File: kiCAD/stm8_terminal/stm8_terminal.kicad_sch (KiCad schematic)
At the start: 26 parts, among them J1 USB_A, J2 PS/2 Female, J3 TV out, SW1 SW_SPST, SW2 local echo, SW3 baud rate 1, SW4 baud rate 0, T1 step down transformer, U1 LD1117V50-TO-220, Y1 20 Mhz

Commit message: Modification à la schématique
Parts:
- removed C2: 100nF, symbol Device:C
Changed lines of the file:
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@@
-    (pin "2")
-  )
-  (symbol (lib_id "Device:C") (at 128.27 114.3 0) (unit 1)
-    (in_bom yes) (on_board yes) (fields_autoplaced)
-    (property "Reference" "C2" (id 0) (at 131.445 113.0299 0)
-      (effects (font (size 1.27 1.27)) (justify left))
-    )
-    (property "Value" "100nF" (id 1) (at 131.445 115.5699 0)
-      (effects (font (size 1.27 1.27)) (justify left))
-    )
-    (property "Footprint" "" (id 2) (at 129.2352 118.11 0)
-      (effects (font (size 1.27 1.27)) hide)
-    )
-    (property "Datasheet" "~" (id 3) (at 128.27 114.3 0)
-      (effects (font (size 1.27 1.27)) hide)
-    )
-    (pin "1")
     (pin "2")
   )
@@
     (pin "1")
   )
-  (symbol (lib_id "power:GND") (at 128.27 118.11 0) (unit 1)
-    (in_bom yes) (on_board yes) (fields_autoplaced)
-    (property "Reference" "#PWR05" (id 0) (at 128.27 124.46 0)
-      (effects (font (size 1.27 1.27)) hide)
-    )
-    (property "Value" "GND" (id 1) (at 128.27 123.19 0))
-    (property "Footprint" "" (id 2) (at 128.27 118.11 0)
-      (effects (font (size 1.27 1.27)) hide)
-    )
-    (property "Datasheet" "" (id 3) (at 128.27 118.11 0)
-      (effects (font (size 1.27 1.27)) hide)
-    )
-    (pin "1")
-  )
   (symbol (lib_id "Device:C_Polarized") (at 112.395 55.88 0) (unit 1)
     (in_bom yes) (on_board yes) (fields_autoplaced)
@@
       (reference "#PWR04") (unit 1) (value "GND") (footprint "")
     )
-    (path "/845855d3-4d0e-4980-8991-a5f84e6b7908"
-      (reference "#PWR05") (unit 1) (value "GND") (footprint "")
-    )
     (path "/d18cab06-a3b9-490f-bba2-3968ae23ef3a"
       (reference "#PWR06") (unit 1) (value "GND") (footprint "")
@@
       (reference "C1") (unit 1) (value "4700µF/25V") (footprint "")
     )
-    (path "/141ad850-4428-4f02-9634-53c9c9f30976"
-      (reference "C2") (unit 1) (value "100nF") (footprint "")
-    )
     (path "/e24a0cb3-c996-41e3-aea6-3ef71e605019"

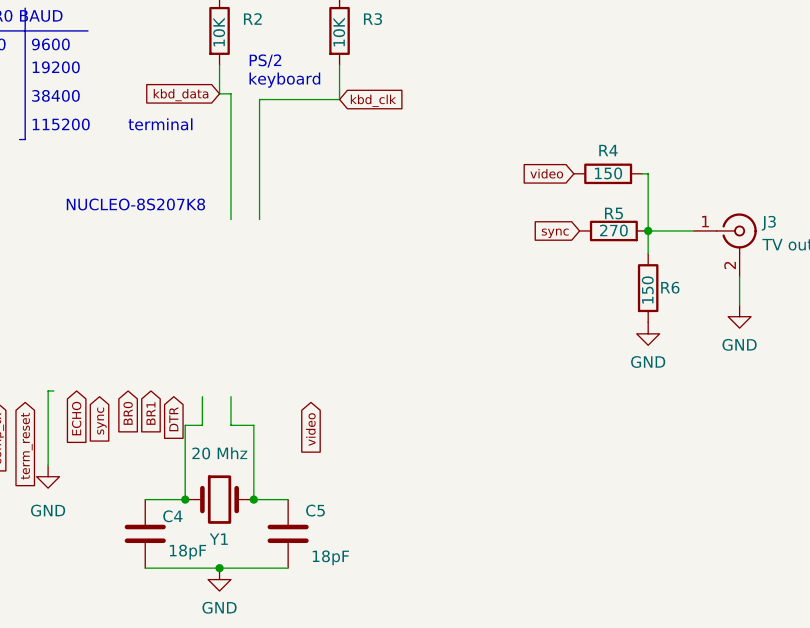
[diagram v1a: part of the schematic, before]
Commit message: mise à jour schématique vers V1.1R0
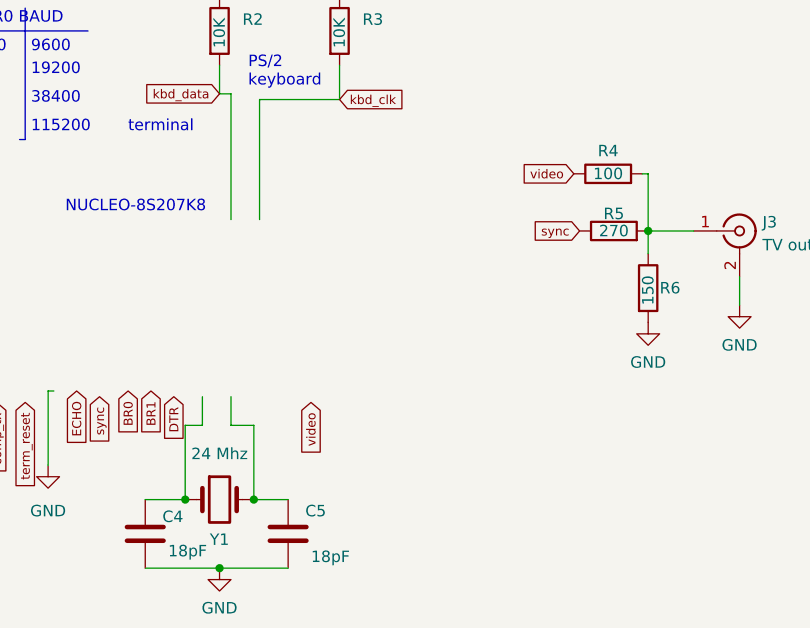
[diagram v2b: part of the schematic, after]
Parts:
- R4: value 150 -> 100
- Y1: value 20 Mhz -> 24 Mhz
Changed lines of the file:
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@@
     (in_bom yes) (on_board yes)
     (property "Reference" "R4" (id 0) (at 254.635 78.74 90))
-    (property "Value" "150" (id 1) (at 254.635 81.28 90))
+    (property "Value" "100" (id 1) (at 254.635 81.28 90))
     (property "Footprint" "" (id 2) (at 254.635 83.058 90)
       (effects (font (size 1.27 1.27)) hide)
@@
     (in_bom yes) (on_board yes)
     (property "Reference" "Y1" (id 0) (at 211.455 121.92 0))
-    (property "Value" "20 Mhz" (id 1) (at 211.455 112.395 0))
+    (property "Value" "24 Mhz" (id 1) (at 211.455 112.395 0))
     (property "Footprint" "" (id 2) (at 211.455 117.475 0)
       (effects (font (size 1.27 1.27)) hide)
@@
     )
     (path "/26747773-3488-4cb1-8229-30ef1aeade7f"
-      (reference "R4") (unit 1) (value "150") (footprint "")
+      (reference "R4") (unit 1) (value "100") (footprint "")
     )
     (path "/b67ff7bf-f5af-4273-8904-9679f573e1a3"
@@
     )
     (path "/a798556e-a1c1-4369-8d5b-478f85bd9f5b"
-      (reference "Y1") (unit 1) (value "20 Mhz") (footprint "")
-    )
-  )
+      (reference "Y1") (unit 1) (value "24 Mhz") (footprint "")
+    )
+  )
